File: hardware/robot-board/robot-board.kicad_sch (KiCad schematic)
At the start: 74 parts, among them J1 USB_C_Receptacle_USB2.0_14P, J2 Conn_01x03_Pin, J3 Conn_01x03_Pin, J4 Conn_01x03_Pin, J5 Conn_01x03_Pin, Q1 BSS138, Q2 BSS138, Q3 BSS138, Q4 BSS138, SW1 SW_SPST, U1 ESP32-S3-WROOM-1, U2 LMR51450, U3 LMR51450, U4 TPS61088, U6 TVS0500DRV

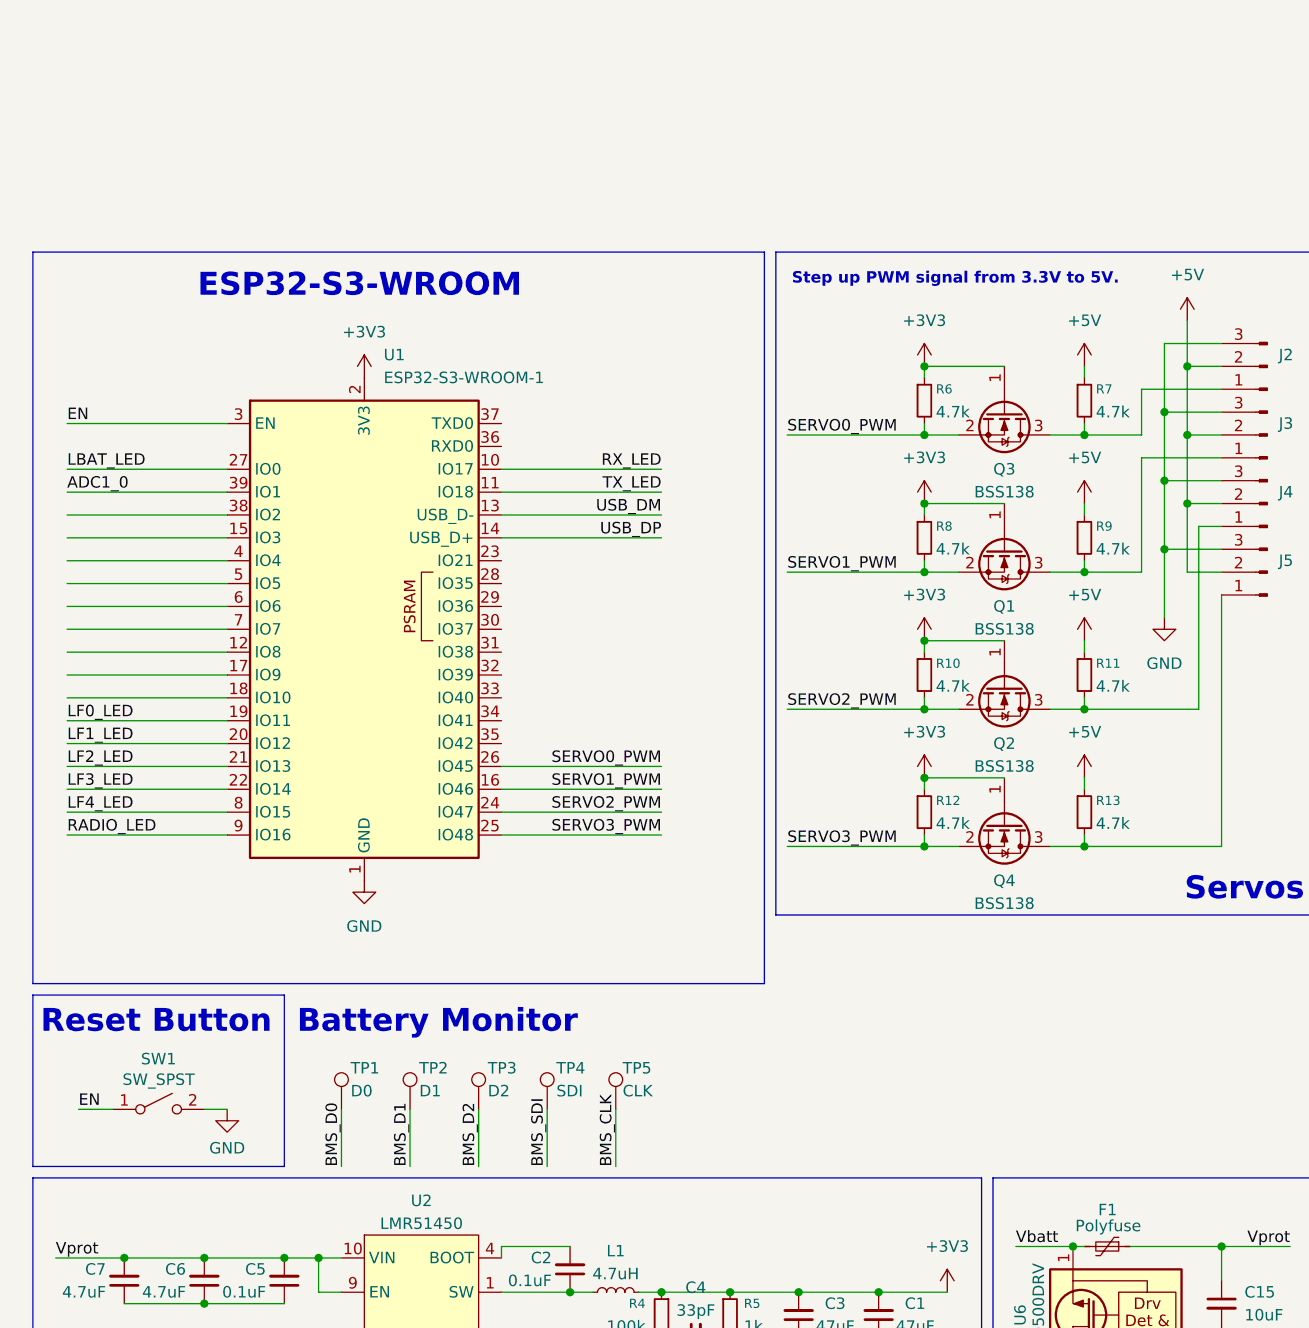
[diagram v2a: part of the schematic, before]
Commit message: Update robot-board.kicad_sch
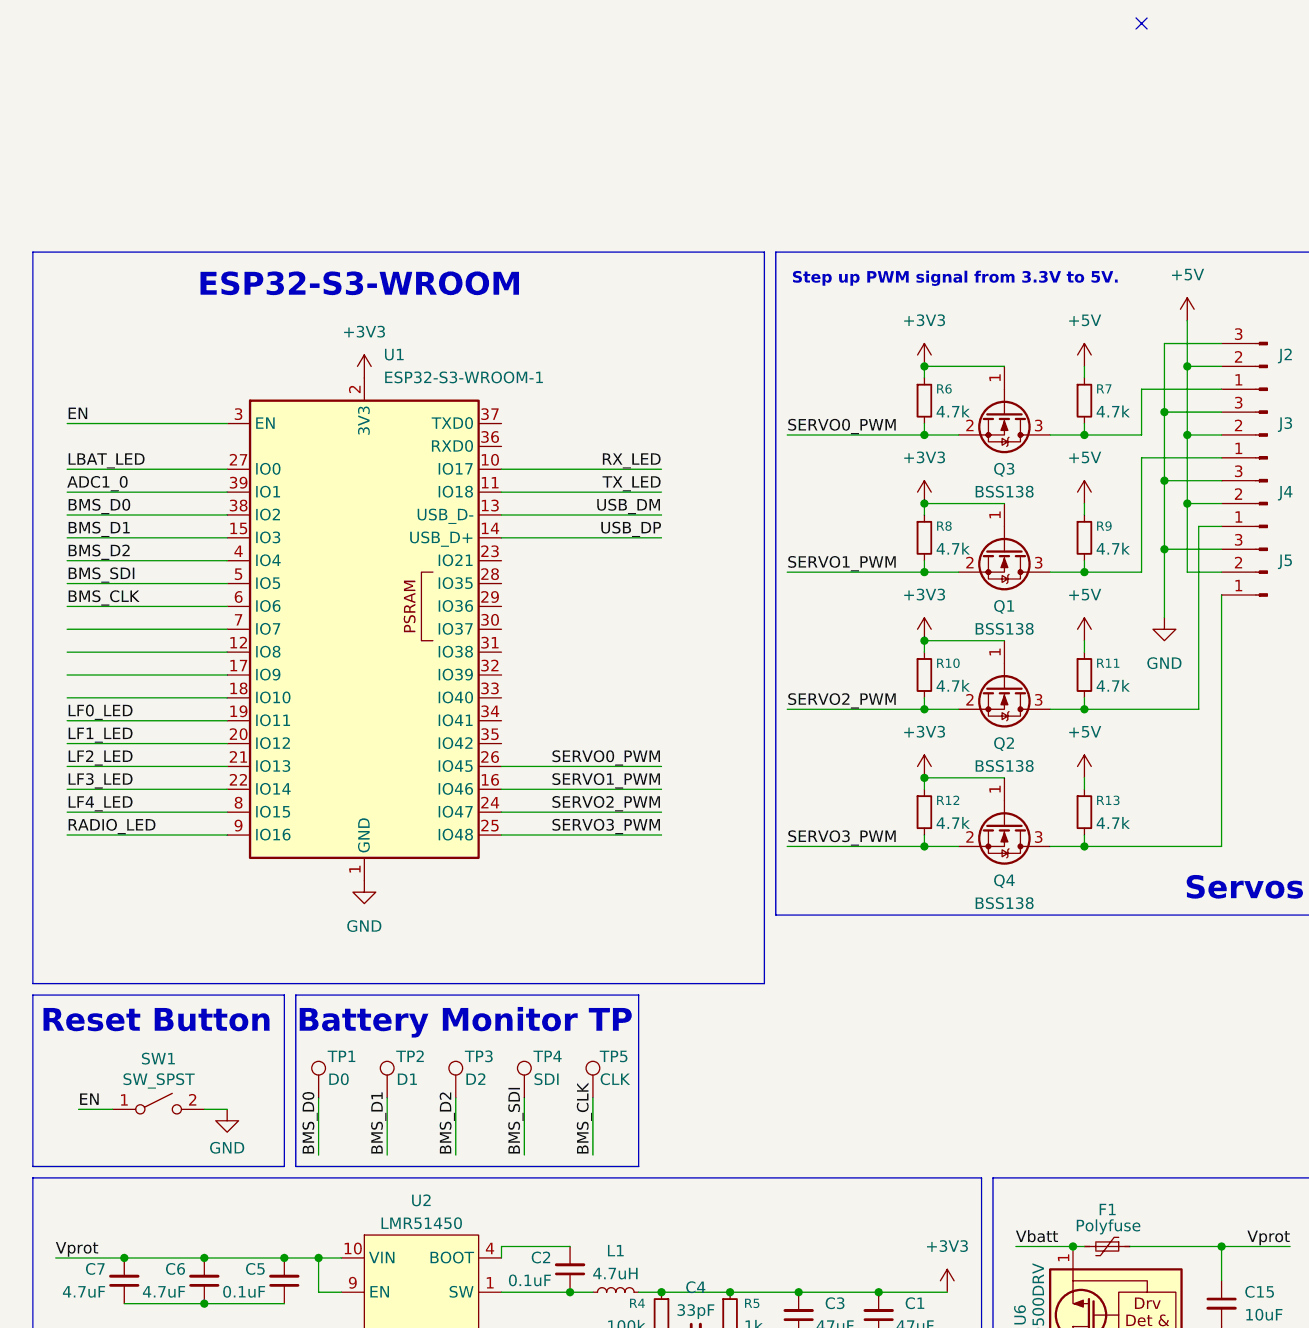
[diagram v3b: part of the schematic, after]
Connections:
- net BMS_CLK: now also U1.6 (IO6)
- net BMS_D0: now also U1.38 (IO2)
- net BMS_D1: now also U1.15 (IO3)
- net BMS_D2: now also U1.4 (IO4)
- net BMS_SDI: now also U1.5 (IO5)
- no-connect marks 3 -> 4
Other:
- note added: "Battery Monitor TP"
- note removed: "Battery Monitor"
- moved on the sheet: TP1, TP2, TP3, TP4, TP5
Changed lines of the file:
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@@
 	)
 	(rectangle
+		(start 41.91 95.25)
+		(end 80.01 114.3)
+		(stroke
+			(width 0)
+			(type default)
+		)
+		(fill
+			(type none)
+		)
+	)
+	(rectangle
 		(start 119.38 146.05)
 		(end 166.37 196.85)
@@
 		)
 	)
-	(text "Battery Monitor"
+	(text "Battery Monitor TP\n"
 		(exclude_from_sim no)
-		(at 57.658 98.298 0)
+		(at 60.706 98.298 0)
 		(effects
 			(font
@@
 	)
 	(no_connect
+		(at 135.89 -12.7)
+	)
+	(no_connect
 		(at 148.59 152.4)
 	)
@@
 	(wire
 		(pts
-			(xy 69.85 114.3) (xy 69.85 107.95)
+			(xy 67.31 113.03) (xy 67.31 106.68)
 		)
 		(stroke
@@
 	(wire
 		(pts
-			(xy 62.23 114.3) (xy 62.23 107.95)
+			(xy 59.69 113.03) (xy 59.69 106.68)
 		)
 		(stroke
@@
 	(wire
 		(pts
-			(xy 46.99 114.3) (xy 46.99 107.95)
+			(xy 44.45 113.03) (xy 44.45 106.68)
 		)
 		(stroke
@@
 	(wire
 		(pts
-			(xy 54.61 114.3) (xy 54.61 107.95)
+			(xy 52.07 113.03) (xy 52.07 106.68)
 		)
 		(stroke
@@
 	(wire
 		(pts
-			(xy 77.47 114.3) (xy 77.47 107.95)
+			(xy 74.93 113.03) (xy 74.93 106.68)
 		)
 		(stroke
@@
 		)
 	)
+	(label "BMS_CLK"
+		(at 16.51 52.07 0)
+		(effects
+			(font
+				(size 1.27 1.27)
+			)
+			(justify left bottom)
+		)
+	)
 	(label "LF4_LED"
 		(at 16.51 74.93 0)
@@
 		)
 	)
+	(label "BMS_D2"
+		(at 16.51 46.99 0)
+		(effects
+			(font
+				(size 1.27 1.27)
+			)
+			(justify left bottom)
+		)
+	)
 	(label "Vprot"
 		(at 15.24 166.37 0)
@@
 	)
 	(label "BMS_D0"
-		(at 46.99 114.3 90)
+		(at 44.45 113.03 90)
 		(effects
 			(font
@@
 		)
 	)
+	(label "BMS_D0"
+		(at 16.51 41.91 0)
+		(effects
+			(font
+				(size 1.27 1.27)
+			)
+			(justify left bottom)
+		)
+	)
 	(label "LF2_LED"
 		(at 16.51 69.85 0)
@@
 	)
 	(label "BMS_D2"
-		(at 62.23 114.3 90)
+		(at 59.69 113.03 90)
 		(effects
 			(font
@@
 		)
 	)
+	(label "BMS_D1"
+		(at 16.51 44.45 0)
+		(effects
+			(font
+				(size 1.27 1.27)
+			)
+			(justify left bottom)
+		)
+	)
 	(label "SERVO3_PWM"
 		(at 96.52 78.74 0)
@@
 		)
 	)
+	(label "BMS_SDI"
+		(at 16.51 49.53 0)
+		(effects
+			(font
+				(size 1.27 1.27)
+			)
+			(justify left bottom)
+		)
+	)
 	(label "SERVO3_PWM"
 		(at 82.55 77.47 180)
@@
 	)
 	(label "BMS_D1"
-		(at 54.61 114.3 90)
+		(at 52.07 113.03 90)
 		(effects
 			(font
@@
 	)
 	(label "BMS_SDI"
-		(at 69.85 114.3 90)
+		(at 67.31 113.03 90)
 		(effects
 			(font
@@
 	)
 	(label "BMS_CLK"
-		(at 77.47 114.3 90)
+		(at 74.93 113.03 90)
 		(effects
 			(font
@@
 	(symbol
 		(lib_id "Connector:TestPoint")
-		(at 77.47 107.95 0)
+		(at 74.93 106.68 0)
 		(unit 1)
 		(exclude_from_sim no)
@@
 		(dnp no)
 		(property "Reference" "TP5"
-			(at 78.232 103.378 0)
+			(at 75.692 102.108 0)
 			(effects
 				(font
@@
 		)
 		(property "Value" "CLK"
-			(at 78.232 105.918 0)
+			(at 75.692 104.648 0)
 			(effects
 				(font
@@
 		)
 		(property "Footprint" "TestPoint:TestPoint_THTPad_2.0x2.0mm_Drill1.0mm"
-			(at 82.55 107.95 0)
+			(at 80.01 106.68 0)
 			(effects
 				(font
@@
 		)
 		(property "Datasheet" "~"
-			(at 82.55 107.95 0)
+			(at 80.01 106.68 0)
 			(effects
 				(font
@@
 		)
 		(property "Description" "test point"
-			(at 77.47 107.95 0)
+			(at 74.93 106.68 0)
 			(effects
 				(font
@@
 	(symbol
 		(lib_id "Connector:TestPoint")
-		(at 62.23 107.95 0)
+		(at 59.69 106.68 0)
 		(unit 1)
 		(exclude_from_sim no)
@@
 		(dnp no)
 		(property "Reference" "TP3"
-			(at 63.246 103.378 0)
+			(at 60.706 102.108 0)
 			(effects
 				(font
@@
 		)
 		(property "Value" "D2"
-			(at 63.246 105.918 0)
+			(at 60.706 104.648 0)
 			(effects
 				(font
@@
 		)
 		(property "Footprint" "TestPoint:TestPoint_THTPad_2.0x2.0mm_Drill1.0mm"
-			(at 67.31 107.95 0)
+			(at 64.77 106.68 0)
 			(effects
 				(font
@@
 		)
 		(property "Datasheet" "~"
-			(at 67.31 107.95 0)
+			(at 64.77 106.68 0)
 			(effects
 				(font
@@
 		)
 		(property "Description" "test point"
-			(at 62.23 107.95 0)
+			(at 59.69 106.68 0)
 			(effects
 				(font
@@
 	(symbol
 		(lib_id "Connector:TestPoint")
-		(at 54.61 107.95 0)
+		(at 52.07 106.68 0)
 		(unit 1)
 		(exclude_from_sim no)
@@
 		(dnp no)
 		(property "Reference" "TP2"
-			(at 55.626 103.378 0)
+			(at 53.086 102.108 0)
 			(effects
 				(font
@@
 		)
 		(property "Value" "D1"
-			(at 55.626 105.918 0)
+			(at 53.086 104.648 0)
 			(effects
 				(font
@@
 		)
 		(property "Footprint" "TestPoint:TestPoint_THTPad_2.0x2.0mm_Drill1.0mm"
-			(at 59.69 107.95 0)
+			(at 57.15 106.68 0)
 			(effects
 				(font
@@
 		)
 		(property "Datasheet" "~"
-			(at 59.69 107.95 0)
+			(at 57.15 106.68 0)
 			(effects
 				(font
@@
 		)
 		(property "Description" "test point"
-			(at 54.61 107.95 0)
+			(at 52.07 106.68 0)
 			(effects
 				(font
@@
 	(symbol
 		(lib_id "Connector:TestPoint")
-		(at 46.99 107.95 0)
+		(at 44.45 106.68 0)
 		(unit 1)
 		(exclude_from_sim no)
@@
 		(dnp no)
 		(property "Reference" "TP1"
-			(at 48.006 103.378 0)
+			(at 45.466 102.108 0)
 			(effects
 				(font
@@
 		)
 		(property "Value" "D0"
-			(at 48.006 105.918 0)
+			(at 45.466 104.648 0)
 			(effects
 				(font
@@
 		)
 		(property "Footprint" "TestPoint:TestPoint_THTPad_2.0x2.0mm_Drill1.0mm"
-			(at 52.07 107.95 0)
+			(at 49.53 106.68 0)
 			(effects
 				(font
@@
 		)
 		(property "Datasheet" "~"
-			(at 52.07 107.95 0)
+			(at 49.53 106.68 0)
 			(effects
 				(font
@@
 		)
 		(property "Description" "test point"
-			(at 46.99 107.95 0)
+			(at 44.45 106.68 0)
 			(effects
 				(font
@@
 	(symbol
 		(lib_id "Connector:TestPoint")
-		(at 69.85 107.95 0)
+		(at 67.31 106.68 0)
 		(unit 1)
 		(exclude_from_sim no)
@@
 		(dnp no)
 		(property "Reference" "TP4"
-			(at 70.866 103.378 0)
+			(at 68.326 102.108 0)
 			(effects
 				(font
@@
 		)
 		(property "Value" "SDI"
-			(at 70.866 105.918 0)
+			(at 68.326 104.648 0)
 			(effects
 				(font
@@
 		)
 		(property "Footprint" "TestPoint:TestPoint_THTPad_2.0x2.0mm_Drill1.0mm"
-			(at 74.93 107.95 0)
+			(at 72.39 106.68 0)
 			(effects
 				(font
@@
 		)
 		(property "Datasheet" "~"
-			(at 74.93 107.95 0)
+			(at 72.39 106.68 0)
 			(effects
 				(font
@@
 		)
 		(property "Description" "test point"
-			(at 69.85 107.95 0)
+			(at 67.31 106.68 0)
 			(effects
 				(font

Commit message: finished most of schematic
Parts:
- removed U4: TPS61088, Package_DFN_QFN:Texas_VQFN-RHL-20_ThermalVias, symbol Regulator_Switching:TPS61088
- added C16, C17, C18, C19, C20, C21, C24, C25, C32: 0.1uF, Capacitor_SMD:C_0402_1005Metric, symbol Device:C_Small
- added C22: 100pF, Capacitor_SMD:C_0402_1005Metric, symbol Device:C_Small
- added C23: 4.7nF, Capacitor_SMD:C_0402_1005Metric, symbol Device:C_Small
- added C26, C27, C28, C29, C30, C31: 22uF, Capacitor_SMD:C_0402_1005Metric, symbol Device:C_Small
- added C33: 4.7uF, Capacitor_SMD:C_0402_1005Metric, symbol Device:C_Small
- added D11: LF5, LED_SMD:LED_1206_3216Metric, symbol Device:LED
- added J10, J11, J8, J9: 1x2_Screw, RedRobotFootprints:ScrewTerminalP3.5mm, symbol Connector:Screw_Terminal_01x02
- added J6: Barrel_Jack, Connector_BarrelJack:BarrelJack_Horizontal, symbol Connector:Barrel_Jack_Switch
- added J7: 1x8_Pin, Connector_PinHeader_2.54mm:PinHeader_1x08_P2.54mm_Vertical_SMD_Pin1Left, symbol Connector:Conn_01x08_Pin
- added L3: 4.7uH, Inductor_SMD:L_Bourns_SRP7028A_7.3x6.6mm, symbol Device:L_Small
- added R27: 54.9k, Resistor_SMD:R_0603_1608Metric, symbol Device:R_Small
- added R28: 11.3k, Resistor_SMD:R_0603_1608Metric, symbol Device:R_Small
- added R29: 1M, Resistor_SMD:R_0603_1608Metric, symbol Device:R_Small
- added R30: 100k, Resistor_SMD:R_0603_1608Metric, symbol Device:R_Small
- added R31: 5.1R, Resistor_SMD:R_0402_1005Metric, symbol Device:R_Small
- added R32: 15k, Resistor_SMD:R_0603_1608Metric, symbol Device:R_Small
- added R33: 6mR, Resistor_SMD:R_0603_1608Metric, symbol Device:R_Small
- added R34: 49.9k, Resistor_SMD:R_0603_1608Metric, symbol Device:R_Small
- added U4, U5: DRV8835, Package_SON:WSON-12-1EP_3x2mm_P0.5mm_EP1x2.65, symbol Driver_Motor:DRV8835
- added U7: TPS552892, symbol Regulator_Switching:TPS552892
- C1, C10, C11, C12, C13, C14, C15, C2, C3, C4, C5, C6, C7, C8, C9: footprint (none) -> Capacitor_SMD:C_0402_1005Metric
- D1, D2, D3, D4, D5: footprint (none) -> LED_SMD:LED_1206_3216Metric
- D10: value RXLED -> LF4; footprint (none) -> LED_SMD:LED_1206_3216Metric
- D6: value LBAT -> LF0; footprint (none) -> LED_SMD:LED_1206_3216Metric
- D7: value RLED -> LF1; footprint (none) -> LED_SMD:LED_1206_3216Metric
- D8: value PWR -> LF2; footprint (none) -> LED_SMD:LED_1206_3216Metric
- D9: value TXLED -> LF3; footprint (none) -> LED_SMD:LED_1206_3216Metric
- J1: footprint (none) -> footprints:USB_C_Receptacle_GCT_USB4105-xx-A_16P_TopMnt_Horizontal
- J2, J3, J4, J5: footprint (none) -> Connector_PinHeader_2.54mm:PinHeader_1x02_P2.54mm_Vertical_SMD_Pin1Right
- L1, L2: footprint (none) -> Inductor_SMD:L_Bourns_SRP7028A_7.3x6.6mm
- R1, R10, R11, R12, R13, R2, R6, R7, R8, R9: footprint (none) -> Resistor_SMD:R_0402_1005Metric
- R14, R15, R16, R3, R4, R5: footprint (none) -> Resistor_SMD:R_0603_1608Metric
- R17: value 330R -> 82R; footprint (none) -> Resistor_SMD:R_0402_1005Metric
- R18, R19, R20, R21, R22, R23, R24, R25, R26: value 18R -> 5.1R; footprint (none) -> Resistor_SMD:R_0402_1005Metric
- SW1: footprint (none) -> random-keyboard-parts:SKQGADE010
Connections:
- net PGND is gone; now on net AGND: C1.1, C13.1, C14.1, C3.1, U2.13 (PGND), U3.13 (PGND)
- net +3V3: now also C17.2, C18.2, J7.2 (Pin_2), U4.11 (MODE), U4.12 (VCC), U5.11 (MODE), U5.12 (VCC), U7.1 (EN/UVLO)
- net ADC1_0: now also C19.2, R29.2, R30.1
- net AGND: now also C21.1, C22.1, C23.1, C26.1, C27.1, C28.1, C29.1, C30.1, C31.1, C32.1, C33.1, R28.2, R34.2, U7.17 (AGND), U7.5 (DITH/SYNC), U7.9 (PGND)
- net GND: now also C16.1, C17.1, C18.1, C19.1, C20.1, D11.1 (K), J6.2, J6.3, J7.1 (Pin_1), R30.2, U4.6 (GND), U5.6 (GND)
- net RADIO_LED: now also U1.23 (IO21); no longer U1.9 (IO16)
- net VIN: no longer C15.1, F1.1
- net MOTOR1_PWM: now reaches U1.12 (IO8)
- net MOTOR1_PWM: now also U5.8 (B_PH)
- net MOTOR2_PWM: now reaches U1.17 (IO9)
- net MOTOR2_PWM: now also U4.10 (A_PH)
- net MOTOR3_PWM: now reaches U1.18 (IO10)
- net MOTOR3_PWM: now also U4.8 (B_PH)
- net MOTOR1_EN: now reaches U1.28 (IO35)
- net MOTOR1_EN: now also U5.7 (B_EN)
- net MOTOR0_EN: now reaches U1.29 (IO36)
- net MOTOR0_EN: now also U5.9 (A_EN)
- net LF0: now reaches U1.30 (IO37)
- net LF0: now also J7.3 (Pin_3)
- net LF1: now reaches U1.31 (IO38)
- net LF1: now also J7.4 (Pin_4)
- net LF2: now reaches U1.32 (IO39)
- net LF2: now also J7.5 (Pin_5)
- net LF3: now reaches U1.33 (IO40)
- net LF3: now also J7.6 (Pin_6)
- net LF4: now reaches U1.34 (IO41)
- net LF4: now also J7.7 (Pin_7)
- net LF5: now reaches U1.35 (IO42)
- net LF5: now also J7.8 (Pin_8)
- net MOTOR2_EN: now reaches U1.36 (RXD0)
- net MOTOR2_EN: now also U4.9 (A_EN)
- net MOTOR3_EN: now reaches U1.37 (TXD0)
- net MOTOR3_EN: now also U4.7 (B_EN)
- net MOTOR0_PWM: now reaches U1.7 (IO7)
- net MOTOR0_PWM: now also U5.10 (A_PH)
- net Vbatt renamed +BATT
- net +BATT: now also J6.1
- new net: R34.1, U7.6 (FSW)
- new net: C25.1, L3.1, U7.10 (SW2)
- new net: C24.1, L3.2, U7.8 (SW1)
- new net: C22.2, R32.1, U7.15 (COMP)
- new net: R27.2, R28.1, U7.14 (FB)
- new net: C26.2, C27.2, C28.2, C29.2, C32.2, R33.2, U7.11 (VOUT), U7.12 (ISP)
- new net: C24.2, U7.20 (BOOT1)
- new net: C33.2, U7.18 (VCC)
- new net: C25.2, U7.19 (BOOT2)
- new net: C23.2, R32.2
- new net: D11.2 (A), R31.2
- new net +7V: C16.2, C20.2, R27.1, R33.1, U4.1 (VMM), U5.1 (VMM), U7.13 (ISN)
- new net LF5_LED: R31.1, U1.9 (IO16)
- new net M0+: J8.2 (Pin_2), U5.3 (A_OUT2)
- new net M0-: J8.1 (Pin_1), U5.2 (A_OUT1)
- new net M1+: J9.2 (Pin_2), U5.5 (B_OUT2)
- new net M1-: J9.1 (Pin_1), U5.4 (B_OUT1)
- new net M2+: J10.2 (Pin_2), U4.3 (A_OUT2)
- new net M2-: J10.1 (Pin_1), U4.2 (A_OUT1)
- new net M3+: J11.2 (Pin_2), U4.5 (B_OUT2)
- new net M3-: J11.1 (Pin_1), U4.4 (B_OUT1)
- new net Vprot: C15.1, C21.2, C30.2, C31.2, F1.1, R29.1, U7.7 (VIN)
- no-connect marks 4 -> 9
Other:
- note added: "5V Regulator (Servos)"
- note added: "7V Regulator (Motors)"
- note added: "AGND and PGND planes should be connected by a small trace"
- note added: "Battery Monitor"
- note added: "Battery Monitor Display"
- note added: "Note that C19 should be placed close to ADC1"
- note added: "Note that C21, C32 (C_hf) should be laid out as close to the V_in and GND pins as possible."
- note added: "Servo PWM"
- note removed: "5V Regulator (servo)"
- note removed: "Battery"
- note removed: "Servos"
- moved on the sheet: C1, C10, C11, C12, C13, C14, C15, C2, C3, C4, C5, C6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

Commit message: fixed a bunch of bs
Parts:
- removed U6: TVS0500DRV, Package_SON:WSON-6-1EP_2x2mm_P0.65mm_EP1x1.6mm, symbol Power_Protection:TVS0500DRV
- added U8: TVS1400DRV, Package_SON:WSON-6-1EP_2x2mm_P0.65mm_EP1x1.6mm, symbol Power_Protection:TVS1400DRV
- D1, D10, D11, D2, D9: JLC P/N (none) -> C5123493; LCSC_PN C5123493 -> (none)
- D3: renamed from D6; JLC P/N (none) -> C5123493; LCSC_PN C5123493 -> (none)
- D4: renamed from D3; JLC P/N (none) -> C5123493; LCSC_PN C5123493 -> (none)
- D5: renamed from D7; JLC P/N (none) -> C5123493; LCSC_PN C5123493 -> (none)
- D6: renamed from D4; JLC P/N (none) -> C5123493; LCSC_PN C5123493 -> (none)
- D7: renamed from D8; JLC P/N (none) -> C5123493; LCSC_PN C5123493 -> (none)
- D8: renamed from D5; JLC P/N (none) -> C5123493; LCSC_PN C5123493 -> (none)
- L1, L3: JLC P/N (none) -> C51933838
- L2: JLC P/N (none) -> C5351382
- R2: renamed from R3; JLC P/N (none) -> C860829
- U5: renamed from U7; footprint (none) -> footprints:VQFN21_RYQ_TEX; JLC P/N (none) -> C22375748
- U6: renamed from U5; JLC P/N (none) -> C82045
- U7: renamed from U4; JLC P/N (none) -> C82045
- renumbered C7 to C1, C12 to C10, C3 to C11, C13 to C12, C1 to C13, C30 to C16, C31 to C17, C33 to C18, C21 to C19, C8 to C2, C19 to C20, C24 to C21, C25 to C22, C17 to C23, C18 to C24, C32 to C25, C16 to C28, C20 to C29, C6 to C3, C28 to C30, C22 to C31, C23 to C32, C29 to C33, C9 to C4, C10 to C6, C2 to C7, C11 to C8, C4 to C9, J7 to J1, J6 to J2, J1 to J3, J2 to J4, J3 to J5, J4 to J6, J5 to J7, Q3 to Q1, Q1 to Q2, Q2 to Q3, R4 to R1, R12 to R10, R7 to R11, R9 to R12, R11 to R13, R13 to R14, R2 to R15, R1 to R16, R18 to R17, R19 to R18, R22 to R19, R17 to R20, R23 to R21, R20 to R22, R34 to R23, R29 to R24, R30 to R25, R24 to R26, R21 to R27, R25 to R28, R26 to R29, R14 to R3, R31 to R30, R32 to R31, R33 to R32, R27 to R33, R28 to R34, R15 to R4, R16 to R6, R6 to R7, R10 to R9
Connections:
- net Vprot is gone; now on net VIN: C15.1, C16.2, C17.2, C19.2, F1.1, R24.1, U5.7 (VIN)
- net +3V3: now also U1.3 (EN)
- net +BATT: now also U8.1 (GND), U8.2 (GND), U8.3 (GND), U8.7 (GND)
- net EN: no longer U1.3 (EN)
- net GND: now also U8.4 (IN), U8.5 (IN), U8.6 (IN)
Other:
- note added: "Note that C19, C25 (C_hf) should be laid out as close to the V_in and GND pins as possible."
- note added: "Note that C6 (C_hf) should be laid out as close to the V_in and GND pins as possible."
- note removed: "Note that C10 (C_hf) should be laid out as close to the V_in and GND pins as possible."
- note removed: "Note that C21, C32 (C_hf) should be laid out as close to the V_in and GND pins as possible."
